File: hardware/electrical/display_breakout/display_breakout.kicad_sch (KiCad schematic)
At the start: 6 parts, among them J1 Conn_02x10_Odd_Even, J2 Conn_01x14_Socket, SW1 RotaryEncoder_Switch, SW2 SW_Push, SW3 SW_Push

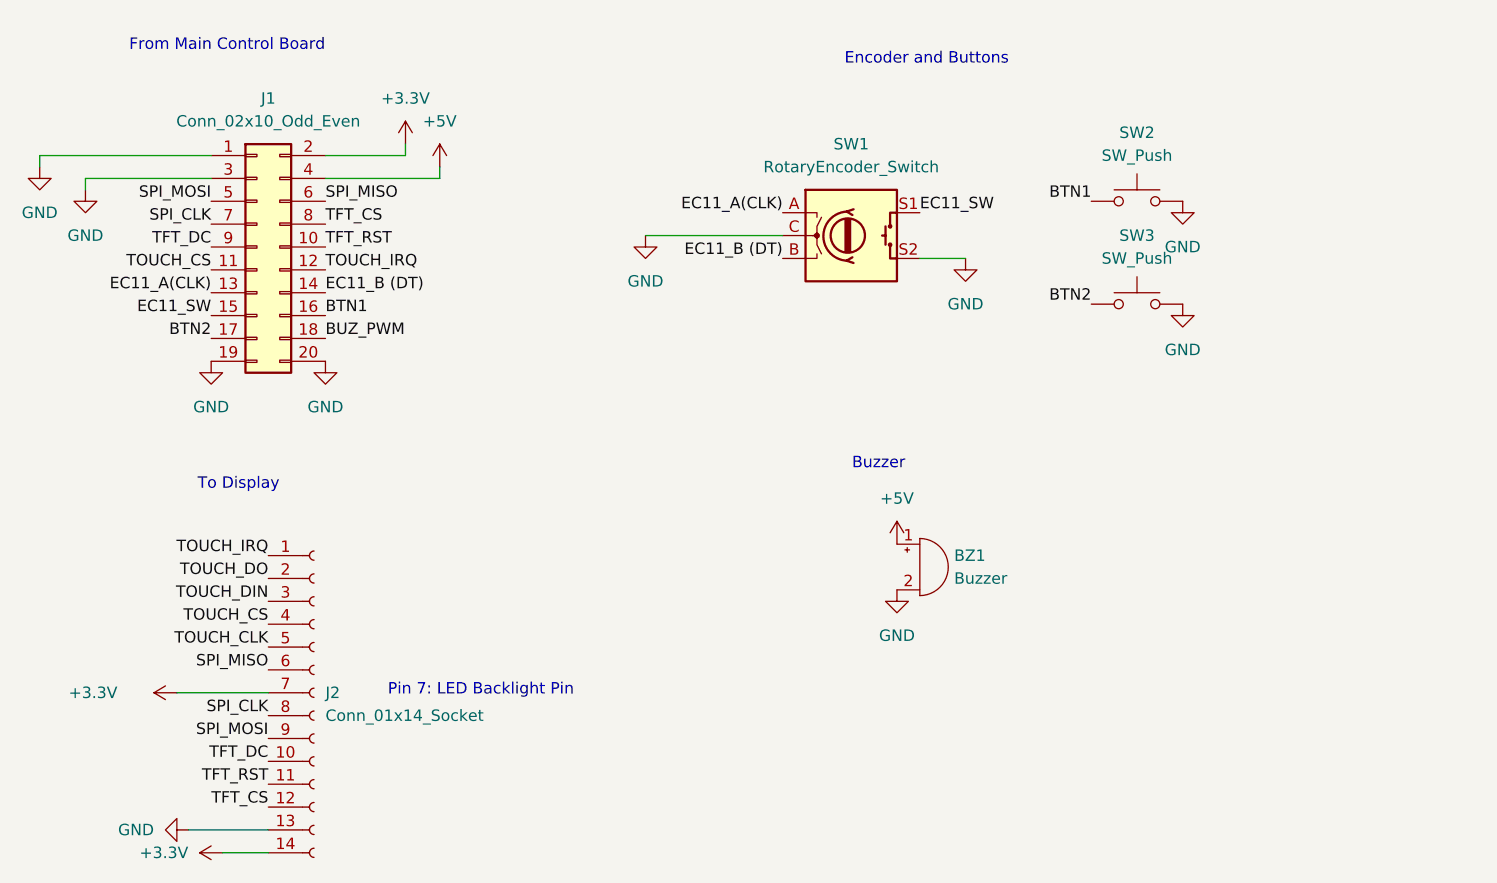
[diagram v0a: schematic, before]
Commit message: updated schematic for display_breakout
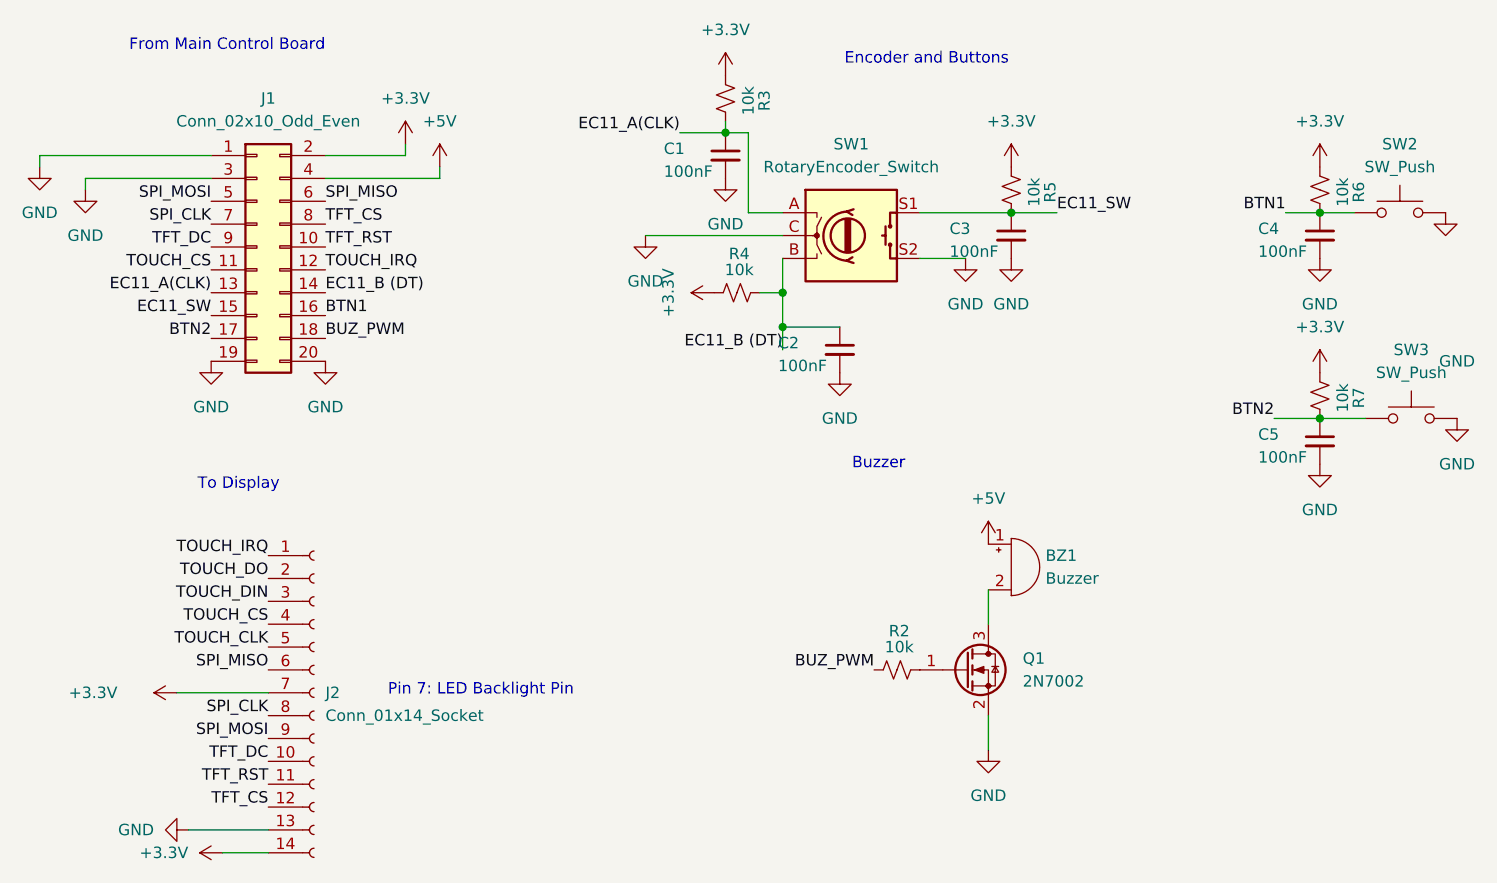
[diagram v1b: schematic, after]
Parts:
- added C1, C2, C3, C4, C5: 100nF, Capacitor_SMD:C_0603_1608Metric, symbol Device:C_Small
- added Q1: 2N7002, Package_TO_SOT_SMD:SOT-23, symbol Transistor_FET:2N7002
- added R2, R3, R4, R5, R6, R7: 10k, Resistor_SMD:R_01005_0402Metric, symbol Device:R_Small_US
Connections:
- net +3.3V: now also R3.2, R4.2, R5.2, R6.2, R7.2
- net BTN1: now also C4.1, R6.1
- net BTN2: now also C5.1, R7.1
- net BUZ_PWM: now also R2.2
- net EC11_A(CLK): now also C1.1, R3.1
- net EC11_B (DT): now also C2.1, R4.1
- net EC11_SW: now also C3.1, R5.1
- net GND: now also C1.2, C2.2, C3.2, C4.2, C5.2, Q1.2 (S); no longer BZ1.2 (-)
- new net: Q1.1 (G), R2.1
- new net: BZ1.2 (-), Q1.3 (D)
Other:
- moved on the sheet: BZ1, SW2, SW3
